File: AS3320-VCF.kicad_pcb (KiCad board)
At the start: 2 copper layers, 26 parts, among them J3 Conn_01x01_Male, J4 Conn_01x01_Male, U1 AS3320

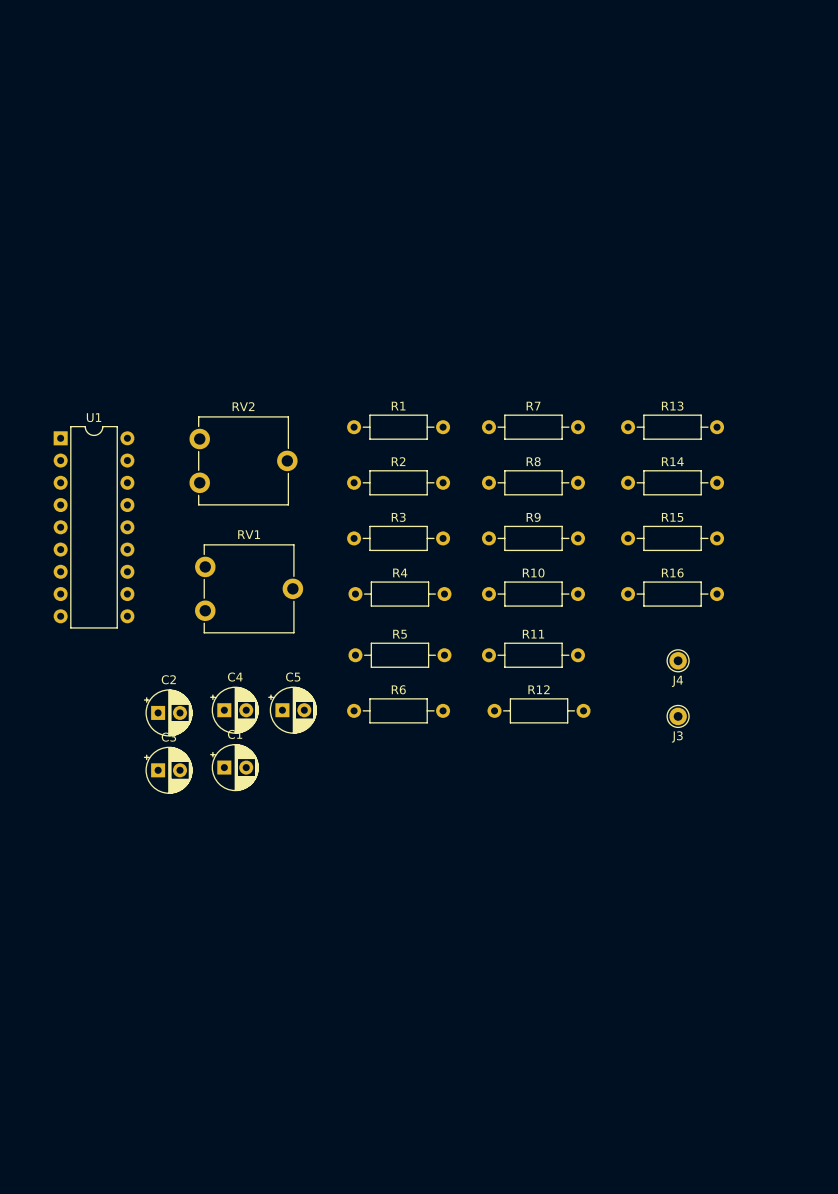
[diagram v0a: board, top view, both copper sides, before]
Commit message: Replace board with new footprints for Audio Jacks and Potentiometers
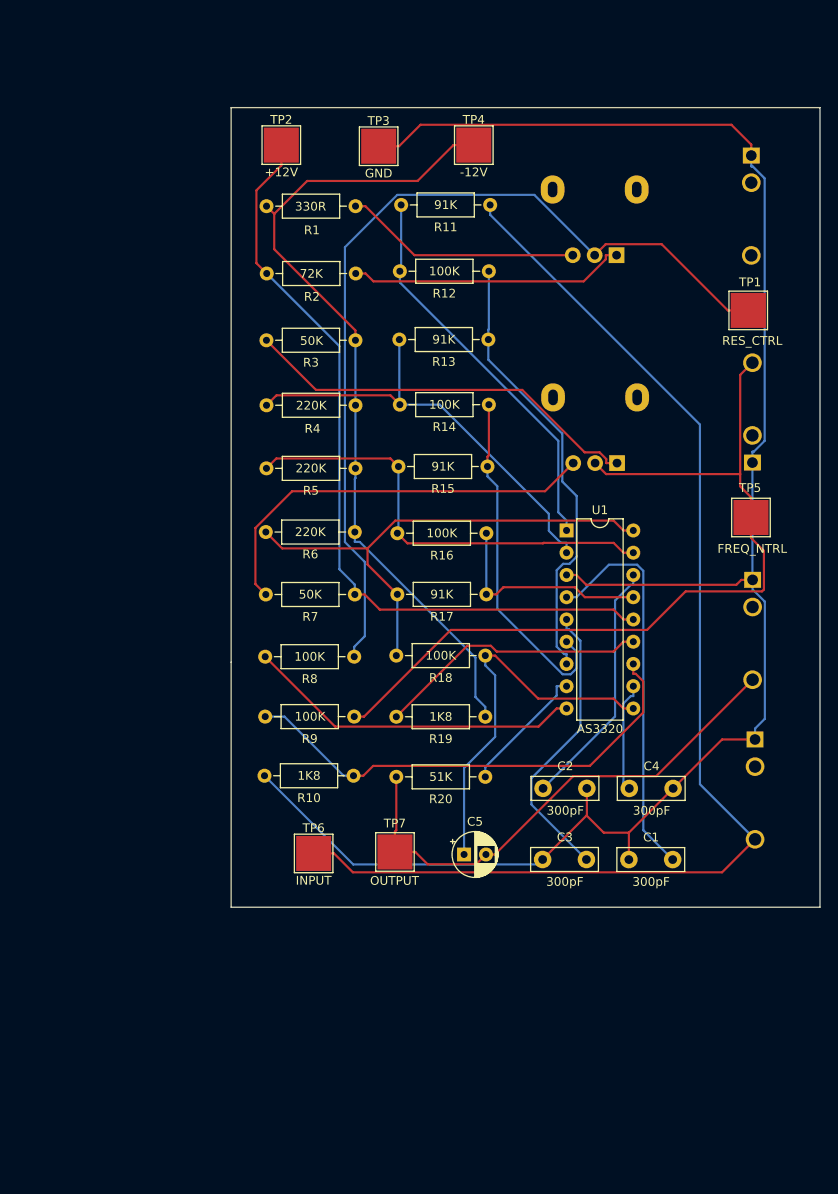
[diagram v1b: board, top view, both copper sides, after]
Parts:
- added J1: AUDIO INPUT, SeattleSynths:Jack_3.5mm_QingPu_WQP-PJ398SM_Vertical_CircularHoles, B.Cu at (185.9, 108.0)
- added J2: RESONANCE CNTL. INPUT, SeattleSynths:Jack_3.5mm_QingPu_WQP-PJ398SM_Vertical_CircularHoles, B.Cu at (185.5, 41.4)
- added R17: 91K, SeattleSynths:R_Axial_DIN0207_L6.3mm_D2.5mm_P10.16mm_Horizontal, F.Cu at (145.1, 91.5)
- added R18: 100K, SeattleSynths:R_Axial_DIN0207_L6.3mm_D2.5mm_P10.16mm_Horizontal, F.Cu at (145.0, 98.5)
- added R19: 1K8, SeattleSynths:R_Axial_DIN0207_L6.3mm_D2.5mm_P10.16mm_Horizontal, F.Cu at (145.0, 105.4)
- added R20: 51K, SeattleSynths:R_Axial_DIN0207_L6.3mm_D2.5mm_P10.16mm_Horizontal, F.Cu at (145.0, 112.3)
- added TP1: RES_CTRL, SeattleSynths:TestPoint_Pad_4.0x4.0mm, F.Cu at (185.2, 59.1)
- added TP2: +12V, SeattleSynths:TestPoint_Pad_4.0x4.0mm, F.Cu at (131.9, 40.2)
- added TP3: GND, SeattleSynths:TestPoint_Pad_4.0x4.0mm, F.Cu at (143.0, 40.3)
- added TP4: -12V, SeattleSynths:TestPoint_Pad_4.0x4.0mm, F.Cu at (153.8, 40.2)
- added TP5: FREQ_NTRL, SeattleSynths:TestPoint_Pad_4.0x4.0mm, F.Cu at (185.5, 82.7)
- added TP6: INPUT, SeattleSynths:TestPoint_Pad_4.0x4.0mm, F.Cu at (135.6, 121.0)
- added TP7: OUTPUT, SeattleSynths:TestPoint_Pad_4.0x4.0mm, F.Cu at (144.8, 120.9)
- C1, C2, C3, C4: footprint Capacitor_THT:CP_Radial_D5.0mm_P2.50mm -> SeattleSynths:C_Disc_D7.5mm_W2.5mm_P5.00mm
- C5: footprint Capacitor_THT:CP_Radial_D5.0mm_P2.50mm -> SeattleSynths:CP_Radial_D5.0mm_P2.50mm
- J3: value Conn_01x01_Male -> FREQ CNTL. INPUT; footprint Connector_Pin:Pin_D1.0mm_L10.0mm -> SeattleSynths:Jack_3.5mm_QingPu_WQP-PJ398SM_Vertical_CircularHoles; moved to B.Cu
- J4: value Conn_01x01_Male -> AUDIO OUTPUT; footprint Connector_Pin:Pin_D1.0mm_L10.0mm -> SeattleSynths:Jack_3.5mm_QingPu_WQP-PJ398SM_Vertical_CircularHoles; moved to B.Cu
- R1: value 100K -> 330R; footprint Resistor_THT:R_Axial_DIN0207_L6.3mm_D2.5mm_P10.16mm_Horizontal -> SeattleSynths:R_Axial_DIN0207_L6.3mm_D2.5mm_P10.16mm_Horizontal
- R10: value 100K -> 1K8; footprint Resistor_THT:R_Axial_DIN0207_L6.3mm_D2.5mm_P10.16mm_Horizontal -> SeattleSynths:R_Axial_DIN0207_L6.3mm_D2.5mm_P10.16mm_Horizontal
- R11, R12, R13, R14, R4, R5, R8: footprint Resistor_THT:R_Axial_DIN0207_L6.3mm_D2.5mm_P10.16mm_Horizontal -> SeattleSynths:R_Axial_DIN0207_L6.3mm_D2.5mm_P10.16mm_Horizontal
- R15: value 1K8 -> 91K; footprint Resistor_THT:R_Axial_DIN0207_L6.3mm_D2.5mm_P10.16mm_Horizontal -> SeattleSynths:R_Axial_DIN0207_L6.3mm_D2.5mm_P10.16mm_Horizontal
- R16: value 51K -> 100K; footprint Resistor_THT:R_Axial_DIN0207_L6.3mm_D2.5mm_P10.16mm_Horizontal -> SeattleSynths:R_Axial_DIN0207_L6.3mm_D2.5mm_P10.16mm_Horizontal
- R2: value 100K -> 72K; footprint Resistor_THT:R_Axial_DIN0207_L6.3mm_D2.5mm_P10.16mm_Horizontal -> SeattleSynths:R_Axial_DIN0207_L6.3mm_D2.5mm_P10.16mm_Horizontal
- R3: value 220K -> 50K; footprint Resistor_THT:R_Axial_DIN0207_L6.3mm_D2.5mm_P10.16mm_Horizontal -> SeattleSynths:R_Axial_DIN0207_L6.3mm_D2.5mm_P10.16mm_Horizontal
- R6: value 1K8 -> 220K; footprint Resistor_THT:R_Axial_DIN0207_L6.3mm_D2.5mm_P10.16mm_Horizontal -> SeattleSynths:R_Axial_DIN0207_L6.3mm_D2.5mm_P10.16mm_Horizontal
- R7: value 91K -> 50K; footprint Resistor_THT:R_Axial_DIN0207_L6.3mm_D2.5mm_P10.16mm_Horizontal -> SeattleSynths:R_Axial_DIN0207_L6.3mm_D2.5mm_P10.16mm_Horizontal
- R9: value 91K -> 100K; footprint Resistor_THT:R_Axial_DIN0207_L6.3mm_D2.5mm_P10.16mm_Horizontal -> SeattleSynths:R_Axial_DIN0207_L6.3mm_D2.5mm_P10.16mm_Horizontal
- RV1, RV2: footprint Potentiometer_THT:Potentiometer_ACP_CA9-V10_Vertical -> SeattleSynths:Potentiometer_Alpha_RD901F-40-00D_Single_Vertical; moved to B.Cu
- U1: footprint Package_DIP:DIP-18_W7.62mm -> SeattleSynths:DIP-18_W7.62mm
- moved RV1 62.1 mm to (170.1, 52.8), turned to 90 degrees
- moved U1 58.7 mm to (164.4, 84.2)
- moved R11 52.4 mm to (145.6, 47.0)
- moved R12 51.3 mm to (145.4, 54.6)
- moved RV2 47.7 mm to (170.2, 76.5), turned to 90 degrees
- moved C1 47.4 mm to (171.5, 121.8)
- moved C4 47.1 mm to (171.6, 113.6)
- moved C3 45.1 mm to (161.7, 121.7)
- moved C2 44.8 mm to (161.7, 113.6)
- moved R10 33.0 mm to (129.9, 112.2)
- moved R9 32.7 mm to (130.0, 105.4)
- moved R8 32.4 mm to (130.0, 98.6)
- moved R7 31.8 mm to (130.1, 91.5)
- moved J3 30.2 mm to (185.7, 76.4)
- moved R13 28.0 mm to (145.3, 62.4)
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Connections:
- C5 pad 2: Net-(C5-Pad2) -> /SIGNAL_OUTPUT
- R1 pad 1: Net-(R1-Pad1) -> -12V
- R1 pad 2: Net-(J3-Pad1) -> Net-(R1-Pad2)
- R10 pad 1: Net-(R10-Pad1) -> GND
- R11 pad 2: Net-(R10-Pad2) -> /SIGNAL_INPUT
- R12 pad 2: Net-(R12-Pad2) -> /OUT1
- R13 pad 2: Net-(R12-Pad2) -> /OUT1
- R14 pad 2: Net-(R14-Pad2) -> /OUT2
- R15 pad 2: -12V -> /OUT2
- R16 pad 1: Net-(C5-Pad2) -> Net-(R15-Pad1)
- R16 pad 2: Net-(R16-Pad2) -> /OUT3
- R2 pad 1: Net-(R2-Pad1) -> +12V
- R2 pad 2: Net-(J4-Pad1) -> Net-(R2-Pad2)
- R3 pad 1: Net-(R10-Pad1) -> Net-(R3-Pad1)
- R4 pad 1: Net-(R11-Pad1) -> Net-(R13-Pad1)
- R5 pad 1: Net-(R13-Pad1) -> Net-(R15-Pad1)
- R6 pad 1: GND -> Net-(R17-Pad1)
- R6 pad 2: Net-(R1-Pad1) -> -12V
- R7 pad 2: Net-(R7-Pad2) -> +12V
- R8 pad 1: Net-(R7-Pad1) -> Net-(R8-Pad1)
- R9 pad 1: Net-(R10-Pad1) -> Net-(R10-Pad2)
- R9 pad 2: Net-(R8-Pad2) -> /FREQ_CTRL_INPUT
- RV1 pad 1: +12V -> Net-(R2-Pad2)
- RV1 pad 2: Net-(R1-Pad1) -> Net-(R8-Pad2)
- RV1 pad 3: GND -> Net-(R1-Pad2)
- RV2 pad 1: +12V -> Net-(R3-Pad1)
- RV2 pad 2: Net-(R2-Pad1) -> /FREQ_CTRL_INPUT
- RV2 pad 3: GND -> Net-(R7-Pad1)
- U1 pad 1: Net-(R7-Pad1) -> Net-(R11-Pad1)
- U1 pad 12: Net-(R1-Pad1) -> Net-(R10-Pad2)
- U1 pad 13: Net-(R15-Pad1) -> Net-(R19-Pad1)
- U1 pad 17: Net-(R11-Pad1) -> Net-(R15-Pad1)
- U1 pad 18: Net-(R13-Pad1) -> Net-(R17-Pad1)
- U1 pad 2: Net-(R10-Pad1) -> Net-(R13-Pad1)
- U1 pad 8: Net-(U1-Pad8) -> /VRES
- U1 pad 9: Net-(R2-Pad1) -> Net-(R8-Pad1)
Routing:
- net GND: track 0.00 -> 211.4 mm
- net /SIGNAL_INPUT: track 0.00 -> 137.8 mm
- net Net-(R8-Pad2): track 0.00 -> 103.2 mm
- net /FREQ_CTRL_INPUT: track 0.00 -> 97.5 mm
- net -12V: track 0.00 -> 95.1 mm
- net +12V: track 0.00 -> 90.1 mm
- net /SIGNAL_OUTPUT: track 0.00 -> 58.8 mm
- net Net-(R17-Pad1): track 0.00 -> 58.2 mm
- net Net-(R10-Pad2): track 0.00 -> 55.1 mm
- net Net-(R15-Pad1): track 0.00 -> 51.5 mm
- net Net-(R13-Pad1): track 0.00 -> 51.4 mm
- net /OUT1: track 0.00 -> 51.0 mm
- net Net-(R7-Pad1): track 0.00 -> 47.4 mm
- net Net-(R3-Pad1): track 0.00 -> 46.1 mm
- net Net-(R11-Pad1): track 0.00 -> 45.1 mm
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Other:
- board outline added: 67.2 x 91.3 mm

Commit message: Replace board with new footprints for Audio Jacks and Potentiometers.
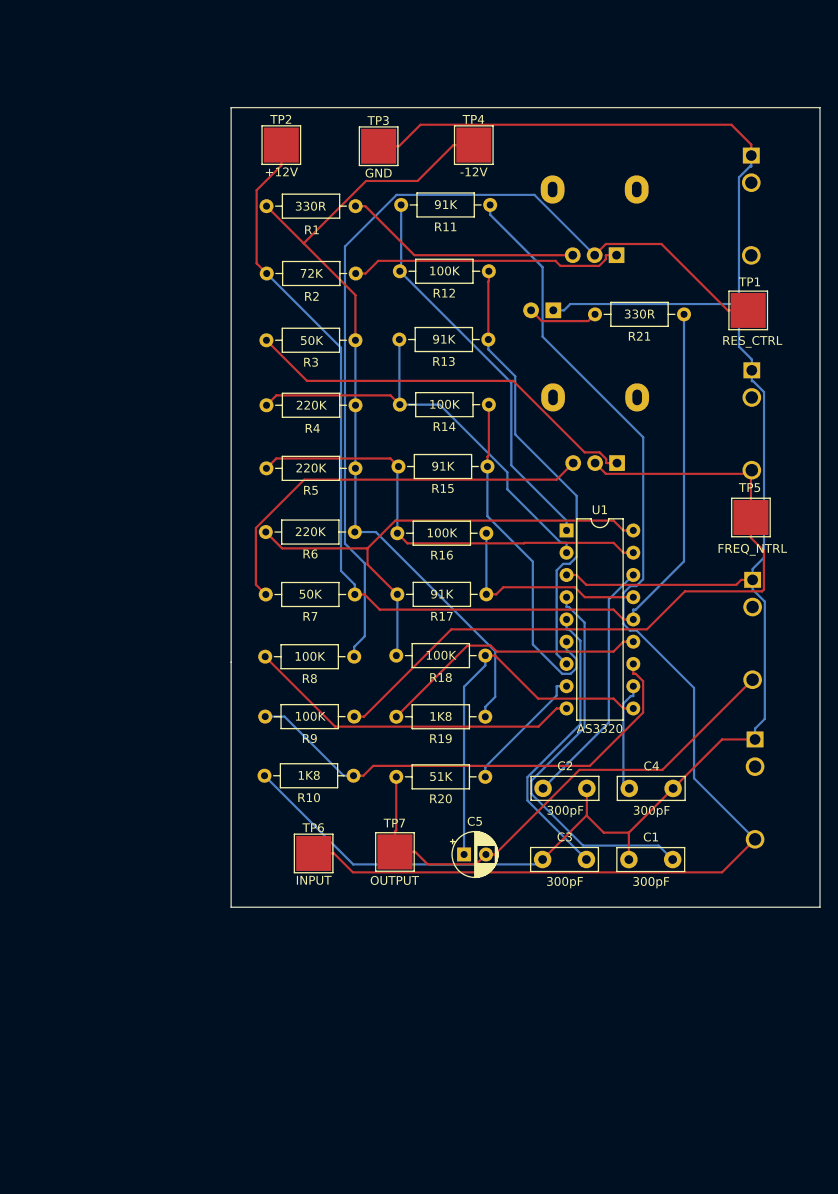
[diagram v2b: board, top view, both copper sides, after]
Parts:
- added D1: LED, SeattleSynths:LED_D5.0mm, B.Cu at (162.9, 59.0)
- added R21: 330R, SeattleSynths:R_Axial_DIN0207_L6.3mm_D2.5mm_P10.16mm_Horizontal, F.Cu at (167.7, 59.5)
- moved J3 10.5 mm to (185.6, 65.9), turned to 180 degrees
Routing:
- net +12V: track 90.1 -> 127.5 mm
- net GND: track 211.4 -> 233.3 mm
- net /FREQ_CTRL_INPUT: track 97.5 -> 85.4 mm
- net Net-(D1-Pad2): track 0.00 -> 8.12 mm
- net /SIGNAL_INPUT: track 137.8 -> 140.5 mm
- net /OUT4: track 44.0 -> 43.1 mm

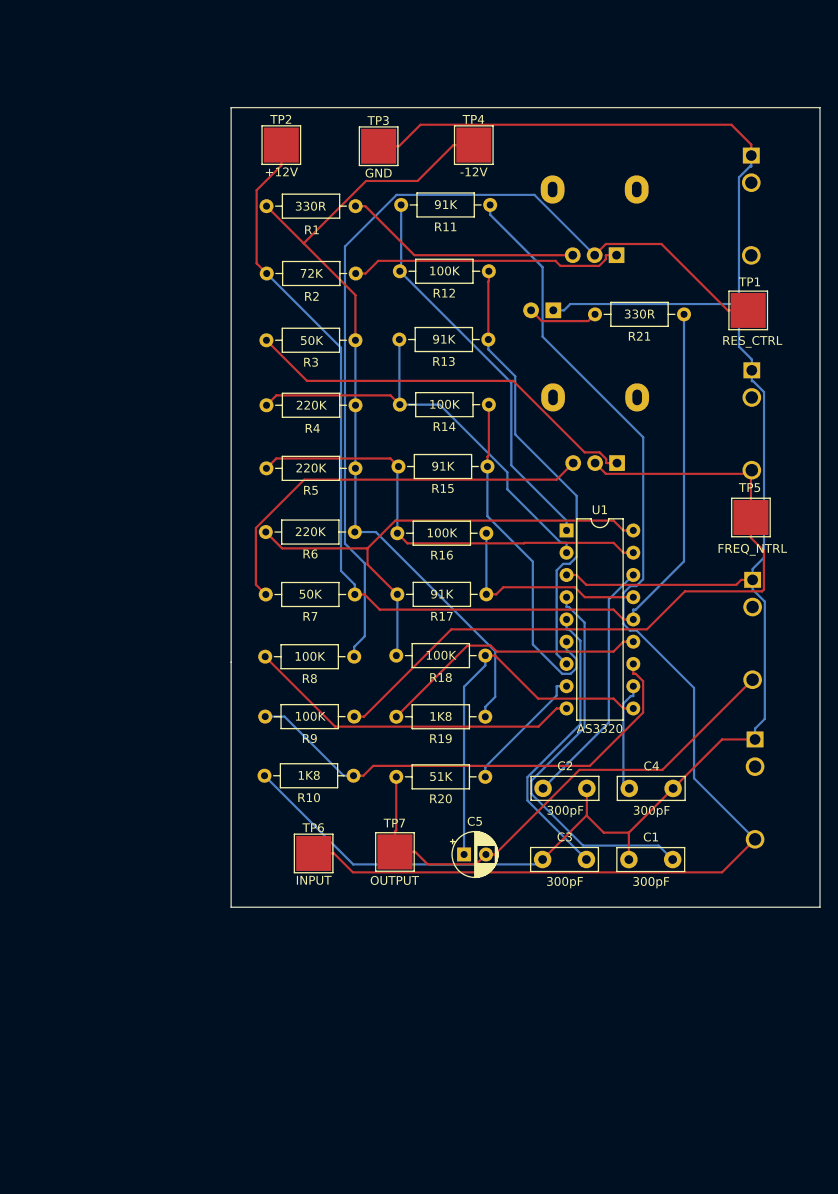
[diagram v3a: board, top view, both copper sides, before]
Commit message: Reroute tracks.
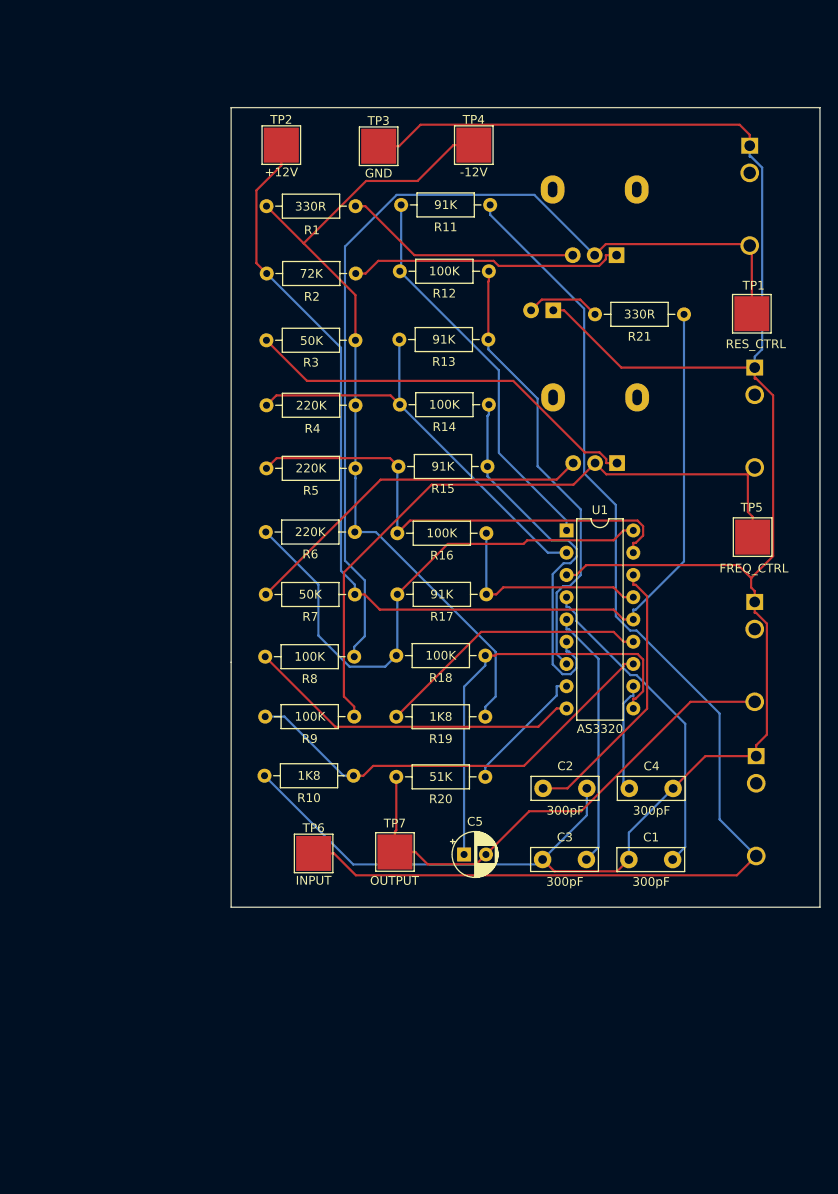
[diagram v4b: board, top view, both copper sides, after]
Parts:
- J1: value AUDIO INPUT -> SIGNAL_INPUT
- J2: value RESONANCE CNTL. INPUT -> RESONANCE_CTRL_INPUT
- J3: value FREQ CNTL. INPUT -> FREQ_CTRL_INPUT
- J4: value AUDIO OUTPUT -> SIGNAL_OUTPUT
- TP5: value FREQ_NTRL -> FREQ_CTRL
- moved J4 2.53 mm to (185.9, 92.3)
- moved TP5 2.25 mm to (185.7, 84.9)
- moved J1 1.90 mm to (186.1, 109.9)
- moved J2 1.13 mm to (185.3, 40.3)
- moved TP1 0.56 mm to (185.6, 59.4)
- moved J3 0.45 mm to (185.9, 65.6)
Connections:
- J2 pad T: (no net) -> /RESONANCE_CTRL_INPUT
- R8 pad 2: Net-(R8-Pad2) -> /RESONANCE_CTRL_INPUT
- RV1 pad 2: Net-(R8-Pad2) -> /RESONANCE_CTRL_INPUT
- TP1 pad 1: Net-(R8-Pad2) -> /RESONANCE_CTRL_INPUT
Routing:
- net /RESONANCE_CTRL_INPUT: track 0.00 -> 108.2 mm
- net Net-(R8-Pad2): track 103.3 -> 0.00 mm
- net GND: track 233.3 -> 245.6 mm
- net Net-(C1-Pad2): track 45.2 -> 36.7 mm
- net /FREQ_CTRL_INPUT: track 85.4 -> 77.3 mm
- net Net-(R7-Pad1): track 47.4 -> 41.3 mm
- net /OUT4: track 43.1 -> 48.3 mm
- net Net-(R10-Pad2): track 55.1 -> 50.3 mm
- net Net-(R15-Pad1): track 51.5 -> 56.2 mm
- net Net-(R17-Pad1): track 58.2 -> 62.2 mm
- net /OUT2: track 39.9 -> 43.8 mm
- net Net-(C3-Pad2): track 33.5 -> 29.7 mm
- net Net-(C2-Pad1): track 28.6 -> 31.7 mm
- net Net-(R13-Pad1): track 51.4 -> 49.6 mm
- net /SIGNAL_OUTPUT: track 58.8 -> 58.0 mm
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
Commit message: Refactor
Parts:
- added BOTTOM_LEFT_MOUNT: MountingHole_3.2mm_M3_Oval, Seattle_Synths:MountingHole_3.2mm_M3_Oval, F.Cu at (109.1, 153.8)
- added BOTTOM_RIGHT_MOUNT: MountingHole_3.2mm_M3_Oval, Seattle_Synths:MountingHole_3.2mm_M3_Oval, F.Cu at (166.1, 154.0)
- added C6: 10uF, Seattle_Synths:CP_Radial_D5.0mm_P2.50mm, F.Cu at (149.6, 128.7)
- added C7: 10uF, Seattle_Synths:CP_Radial_D5.0mm_P2.50mm, F.Cu at (154.1, 45.4)
- added J5: -----, Seattle_Synths:PinHeader_2x05_P2.54mm_Vertical, F.Cu at (165.0, 48.9)
- added TOP_LEFT_MOUNT: MountingHole_3.2mm_M3_Oval, Seattle_Synths:MountingHole_3.2mm_M3_Oval, F.Cu at (109.2, 28.8)
- added TOP_RIGHT_MOUNT: MountingHole_3.2mm_M3_Oval, Seattle_Synths:MountingHole_3.2mm_M3_Oval, F.Cu at (166.0, 28.8)
- C1, C2, C3, C4: footprint SeattleSynths:C_Disc_D7.5mm_W2.5mm_P5.00mm -> Seattle_Synths:C_Disc_D7.5mm_W2.5mm_P5.00mm
- C5: footprint SeattleSynths:CP_Radial_D5.0mm_P2.50mm -> Seattle_Synths:CP_Radial_D5.0mm_P2.50mm
- D1: footprint SeattleSynths:LED_D5.0mm -> Seattle_Synths:LED_D5.0mm
- J1, J2, J3, J4: footprint SeattleSynths:Jack_3.5mm_QingPu_WQP-PJ398SM_Vertical_CircularHoles -> Seattle_Synths:Jack_3.5mm_QingPu_WQP-PJ398SM_Vertical_CircularHoles
- R1, R10, R11, R12, R13, R14, R15, R16, R17, R18, R19, R2, R20, R21, R3, R4, R5, R6, R7, R8, R9: footprint SeattleSynths:R_Axial_DIN0207_L6.3mm_D2.5mm_P10.16mm_Horizontal -> Seattle_Synths:R_Axial_DIN0207_L6.3mm_D2.5mm_P10.16mm_Horizontal
- RV1, RV2: footprint SeattleSynths:Potentiometer_Alpha_RD901F-40-00D_Single_Vertical -> Seattle_Synths:Potentiometer_Alpha_RD901F-40-00D_Single_Vertical
- TP1, TP2, TP5, TP6, TP7: footprint SeattleSynths:TestPoint_Pad_4.0x4.0mm -> Seattle_Synths:TestPoint_Pad_4.0x4.0mm
- TP3: value GND -> -12V; footprint SeattleSynths:TestPoint_Pad_4.0x4.0mm -> Seattle_Synths:TestPoint_Pad_4.0x4.0mm
- TP4: value -12V -> GND; footprint SeattleSynths:TestPoint_Pad_4.0x4.0mm -> Seattle_Synths:TestPoint_Pad_4.0x4.0mm
- U1: footprint SeattleSynths:DIP-18_W7.62mm -> Seattle_Synths:DIP-18_W7.62mm_Socket
- moved TP4 111.0 mm to (125.2, 147.4)
- moved TP3 110.3 mm to (117.1, 147.5)
- moved TP2 107.3 mm to (133.2, 147.5)
- moved TP1 101.9 mm to (121.0, 138.2)
- moved TP5 76.9 mm to (130.2, 138.2)
- moved J2 74.3 mm to (129.9, 89.7)
- moved R21 68.9 mm to (158.0, 127.8)
- moved J4 58.2 mm to (129.9, 108.0)
- moved D1 52.2 mm to (113.8, 41.4)
- moved J3 45.4 mm to (147.5, 89.7)
- moved U1 43.5 mm to (126.8, 62.5), turned to 90 degrees
- moved RV2 41.3 mm to (140.6, 47.6)
- moved RV1 41.1 mm to (140.5, 81.2)
- moved J1 39.0 mm to (147.2, 107.9)
- moved C1 28.8 mm to (156.0, 146.0)
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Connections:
- TP3 pad 1: GND -> -12V
- TP4 pad 1: -12V -> GND
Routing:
- net -12V: track 95.1 -> 231.8 mm
- net Net-(D1-Pad2): track 8.51 -> 130.4 mm, vias 0 -> 1
- net +12V: track 127.5 -> 234.3 mm
- net Net-(C4-Pad1): track 12.6 -> 91.4 mm
- net Net-(C1-Pad2): track 36.7 -> 102.6 mm
- net Net-(R17-Pad1): track 62.2 -> 127.1 mm
- net Net-(C3-Pad2): track 29.7 -> 89.4 mm
- net Net-(C2-Pad1): track 31.7 -> 89.0 mm
- net /VRES: track 14.8 -> 68.6 mm
- net Net-(R15-Pad1): track 56.2 -> 109.3 mm
- net /OUT4: track 48.3 -> 100.4 mm
- net /FREQ_CTRL_INPUT: track 77.3 -> 128.9 mm
- net Net-(R10-Pad2): track 50.3 -> 101.0 mm
- net /OUT3: track 24.6 -> 69.1 mm
- net Net-(R8-Pad1): track 38.6 -> 83.1 mm
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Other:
- board size 67.2 x 91.3 mm -> 71.2 x 131.1 mm
- board text added: "Seattle Synths SS-VCF-1 Rev. 1 [2020-11-08]"
- board text added: "This machine kills fascists."
